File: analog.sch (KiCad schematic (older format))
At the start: 17 parts

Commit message: Erste fertige Version
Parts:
- removed D? (x2): D_Small, symbol Device:D_Small
- removed J?: Conn_02x04_Counter_Clockwise, symbol Connector_Generic:Conn_02x04_Counter_Clockwise
- added D? (x2): D_Schottky_Small, symbol Device:D_Schottky_Small
- added J?: Conn_02x05_Odd_Even, symbol Connector_Generic:Conn_02x05_Odd_Even
- added R? (x2): 10k, symbol Device:R_Small
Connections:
- net labels added: +BATT
- wire segments 43 -> 49
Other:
- moved on the sheet: R?
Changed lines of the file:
@@
 $Descr A4 11693 8268
 encoding utf-8
-Sheet 10 10
+Sheet 9 10
 Title ""
 Date ""
@@
 Wire Wire Line
 	5300 2100 3100 2100
-Wire Wire Line
-	3000 2000 5300 2000
 Connection ~ 3000 2000
-Text HLabel 6050 4750 2    50   UnSpc ~ 0
+Text HLabel 6050 4850 2    50   UnSpc ~ 0
 analog
 $Comp
@@
 	2650 4800 2650 5050
 $Comp
-L Connector_Generic:Conn_02x04_Counter_Clockwise J?
-U 1 1 5F03AAFB
-P 5150 4550
-F 0 "J?" H 5200 4867 50  0000 C CNN
-F 1 "Conn_02x04_Counter_Clockwise" H 5200 4776 50  0000 C CNN
-F 2 "" H 5150 4550 50  0001 C CNN
-F 3 "~" H 5150 4550 50  0001 C CNN
-	1    5150 4550
-	1    0    0    -1
-$EndComp
-Wire Wire Line
-	5450 4450 5450 4550
-Wire Wire Line
-	5450 4750 6050 4750
-Connection ~ 5450 4550
-Wire Wire Line
-	5450 4550 5450 4650
-Connection ~ 5450 4650
-Wire Wire Line
-	5450 4650 5450 4750
-Connection ~ 5450 4750
-$Comp
 L power:+3.3V #PWR?
 U 1 1 5F040190
-P 3550 4100
-F 0 "#PWR?" H 3550 3950 50  0001 C CNN
-F 1 "+3.3V" H 3565 4273 50  0000 C CNN
-F 2 "" H 3550 4100 50  0001 C CNN
-F 3 "" H 3550 4100 50  0001 C CNN
-	1    3550 4100
+P 3400 4100
+F 0 "#PWR?" H 3400 3950 50  0001 C CNN
+F 1 "+3.3V" H 3415 4273 50  0000 C CNN
+F 2 "" H 3400 4100 50  0001 C CNN
+F 3 "" H 3400 4100 50  0001 C CNN
+	1    3400 4100
 	1    0    0    -1
 $EndComp
@@
 L power:GND #PWR?
 U 1 1 5F04055D
-P 4000 5050
-F 0 "#PWR?" H 4000 4800 50  0001 C CNN
-F 1 "GND" H 4005 4877 50  0000 C CNN
-F 2 "" H 4000 5050 50  0001 C CNN
-F 3 "" H 4000 5050 50  0001 C CNN
-	1    4000 5050
-	1    0    0    -1
-$EndComp
-Wire Wire Line
-	4000 5050 4000 4550
-Wire Wire Line
-	4000 4550 4950 4550
+P 4450 5050
+F 0 "#PWR?" H 4450 4800 50  0001 C CNN
+F 1 "GND" H 4455 4877 50  0000 C CNN
+F 2 "" H 4450 5050 50  0001 C CNN
+F 3 "" H 4450 5050 50  0001 C CNN
+	1    4450 5050
+	1    0    0    -1
+$EndComp
+Wire Wire Line
+	4450 5050 4450 4850
 $Comp
 L Device:R_Small R?
 U 1 1 5F04265B
-P 3550 4250
-F 0 "R?" H 3609 4296 50  0000 L CNN
-F 1 "10k" H 3609 4205 50  0000 L CNN
-F 2 "" H 3550 4250 50  0001 C CNN
-F 3 "~" H 3550 4250 50  0001 C CNN
-	1    3550 4250
+P 3400 4250
+F 0 "R?" H 3459 4296 50  0000 L CNN
+F 1 "10k" H 3459 4205 50  0000 L CNN
+F 2 "" H 3400 4250 50  0001 C CNN
+F 3 "~" H 3400 4250 50  0001 C CNN
+	1    3400 4250
 	1    0    0    -1
 $EndComp
@@
 L Device:R_Small R?
 U 1 1 5F04298B
-P 3550 4800
-F 0 "R?" H 3609 4846 50  0000 L CNN
-F 1 "10k" H 3609 4755 50  0000 L CNN
-F 2 "" H 3550 4800 50  0001 C CNN
-F 3 "~" H 3550 4800 50  0001 C CNN
-	1    3550 4800
-	1    0    0    -1
-$EndComp
-Wire Wire Line
-	3550 4350 3550 4450
-Wire Wire Line
-	4950 4450 3550 4450
-Connection ~ 3550 4450
-Wire Wire Line
-	3550 4450 3550 4700
-Wire Wire Line
-	3550 4100 3550 4150
+P 3400 4800
+F 0 "R?" H 3459 4846 50  0000 L CNN
+F 1 "10k" H 3459 4755 50  0000 L CNN
+F 2 "" H 3400 4800 50  0001 C CNN
+F 3 "~" H 3400 4800 50  0001 C CNN
+	1    3400 4800
+	1    0    0    -1
+$EndComp
+Wire Wire Line
+	3400 4350 3400 4450
+Connection ~ 3400 4450
+Wire Wire Line
+	3400 4450 3400 4700
+Wire Wire Line
+	3400 4100 3400 4150
 Wire Wire Line
 	2650 4350 2650 4500
-Wire Wire Line
-	2800 4650 4950 4650
 $Comp
 L power:GND #PWR?
 U 1 1 5F051697
-P 3550 5050
-F 0 "#PWR?" H 3550 4800 50  0001 C CNN
-F 1 "GND" H 3555 4877 50  0000 C CNN
-F 2 "" H 3550 5050 50  0001 C CNN
-F 3 "" H 3550 5050 50  0001 C CNN
-	1    3550 5050
-	1    0    0    -1
-$EndComp
-Wire Wire Line
-	3550 5050 3550 4900
+P 3400 5050
+F 0 "#PWR?" H 3400 4800 50  0001 C CNN
+F 1 "GND" H 3405 4877 50  0000 C CNN
+F 2 "" H 3400 5050 50  0001 C CNN
+F 3 "" H 3400 5050 50  0001 C CNN
+	1    3400 5050
+	1    0    0    -1
+$EndComp
+Wire Wire Line
+	3400 5050 3400 4900
 $Comp
 L Device:R_Small R?
@@
 	1    0    0    -1
 $EndComp
-$Comp
-L Device:D_Small D?
-U 1 1 5F05DB9E
-P 3250 5650
-F 0 "D?" V 3204 5720 50  0000 L CNN
-F 1 "D_Small" V 3295 5720 50  0000 L CNN
-F 2 "" V 3250 5650 50  0001 C CNN
-F 3 "~" V 3250 5650 50  0001 C CNN
-	1    3250 5650
-	0    1    1    0
-$EndComp
-$Comp
-L Device:D_Small D?
-U 1 1 5F05E873
-P 3250 6050
-F 0 "D?" V 3204 6120 50  0000 L CNN
-F 1 "D_Small" V 3295 6120 50  0000 L CNN
-F 2 "" V 3250 6050 50  0001 C CNN
-F 3 "~" V 3250 6050 50  0001 C CNN
-	1    3250 6050
-	0    1    1    0
-$EndComp
 Wire Wire Line
 	3100 5850 3250 5850
@@
 $EndComp
 Wire Wire Line
-	3250 5850 4500 5850
-Wire Wire Line
-	4500 5850 4500 4750
-Wire Wire Line
-	4500 4750 4950 4750
+	3250 5850 4000 5850
+Wire Wire Line
+	4000 5850 4000 4750
 Wire Wire Line
 	2250 5850 2650 5850
@@
 	1    0    0    -1
 $EndComp
+$Comp
+L Connector_Generic:Conn_02x05_Odd_Even J?
+U 1 1 5F2EDB44
+P 5150 4650
+F 0 "J?" H 5200 5067 50  0000 C CNN
+F 1 "Conn_02x05_Odd_Even" H 5200 4976 50  0000 C CNN
+F 2 "" H 5150 4650 50  0001 C CNN
+F 3 "~" H 5150 4650 50  0001 C CNN
+	1    5150 4650
+	1    0    0    -1
+$EndComp
+Wire Wire Line
+	5450 4650 5450 4750
+Connection ~ 5450 4750
+Wire Wire Line
+	5450 4450 5450 4550
+Wire Wire Line
+	5450 4750 5450 4850
+Connection ~ 5450 4550
+Wire Wire Line
+	5450 4550 5450 4650
+Connection ~ 5450 4650
+Wire Wire Line
+	5450 4850 6050 4850
+Connection ~ 5450 4850
+$Comp
+L Device:R_Small R?
+U 1 1 5F2F92B1
+P 3000 4250
+F 0 "R?" H 3059 4296 50  0000 L CNN
+F 1 "10k" H 3059 4205 50  0000 L CNN
+F 2 "" H 3000 4250 50  0001 C CNN
+F 3 "~" H 3000 4250 50  0001 C CNN
+	1    3000 4250
+	1    0    0    -1
+$EndComp
+$Comp
+L Device:R_Small R?
+U 1 1 5F2F92B7
+P 3000 4800
+F 0 "R?" H 3059 4846 50  0000 L CNN
+F 1 "10k" H 3059 4755 50  0000 L CNN
+F 2 "" H 3000 4800 50  0001 C CNN
+F 3 "~" H 3000 4800 50  0001 C CNN
+	1    3000 4800
+	1    0    0    -1
+$EndComp
+Wire Wire Line
+	3000 4100 3000 4150
+$Comp
+L power:GND #PWR?
+U 1 1 5F2F92C3
+P 3000 5050
+F 0 "#PWR?" H 3000 4800 50  0001 C CNN
+F 1 "GND" H 3005 4877 50  0000 C CNN
+F 2 "" H 3000 5050 50  0001 C CNN
+F 3 "" H 3000 5050 50  0001 C CNN
+	1    3000 5050
+	1    0    0    -1
+$EndComp
+Wire Wire Line
+	3000 5050 3000 4900
+Wire Wire Line
+	3000 4350 3000 4550
+Wire Wire Line
+	4450 4850 4950 4850
+Wire Wire Line
+	4000 4750 4950 4750
+Wire Wire Line
+	3400 4450 4950 4450
+Wire Wire Line
+	4950 4550 3000 4550
+Connection ~ 3000 4550
+Wire Wire Line
+	3000 4550 3000 4700
+$Comp
+L power:+BATT #PWR?
+U 1 1 5F30C3D0
+P 3000 4100
+F 0 "#PWR?" H 3000 3950 50  0001 C CNN
+F 1 "+BATT" H 3015 4273 50  0000 C CNN
+F 2 "" H 3000 4100 50  0001 C CNN
+F 3 "" H 3000 4100 50  0001 C CNN
+	1    3000 4100
+	1    0    0    -1
+$EndComp
+$Comp
+L Device:D_Schottky_Small D?
+U 1 1 5F30DD96
+P 3250 6050
+F 0 "D?" V 3250 6120 50  0000 L CNN
+F 1 "D_Schottky_Small" V 3295 6120 50  0001 L CNN
+F 2 "" V 3250 6050 50  0001 C CNN
+F 3 "~" V 3250 6050 50  0001 C CNN
+	1    3250 6050
+	0    1    1    0
+$EndComp
+$Comp
+L Device:D_Schottky_Small D?
+U 1 1 5F30E51F
+P 3250 5650
+F 0 "D?" V 3250 5720 50  0000 L CNN
+F 1 "D_Schottky_Small" V 3295 5720 50  0001 L CNN
+F 2 "" V 3250 5650 50  0001 C CNN
+F 3 "~" V 3250 5650 50  0001 C CNN
+	1    3250 5650
+	0    1    1    0
+$EndComp
+Wire Wire Line
+	2800 4650 4950 4650
+Wire Wire Line
+	3000 2000 5300 2000
 $EndSCHEMATC

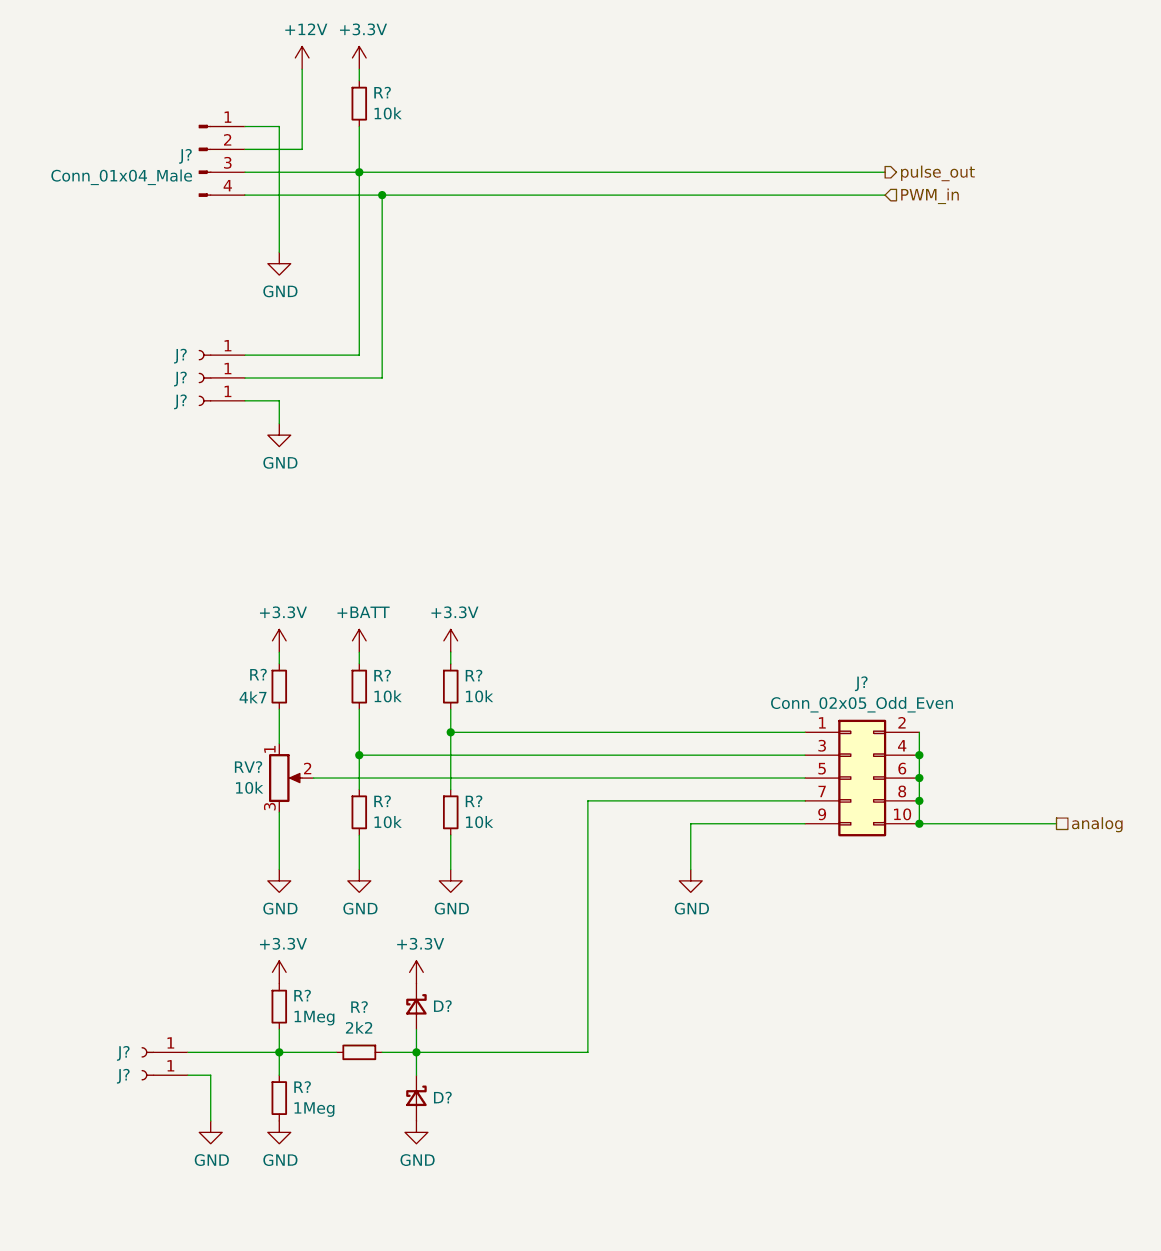
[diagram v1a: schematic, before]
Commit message: Bauteile grob platziert
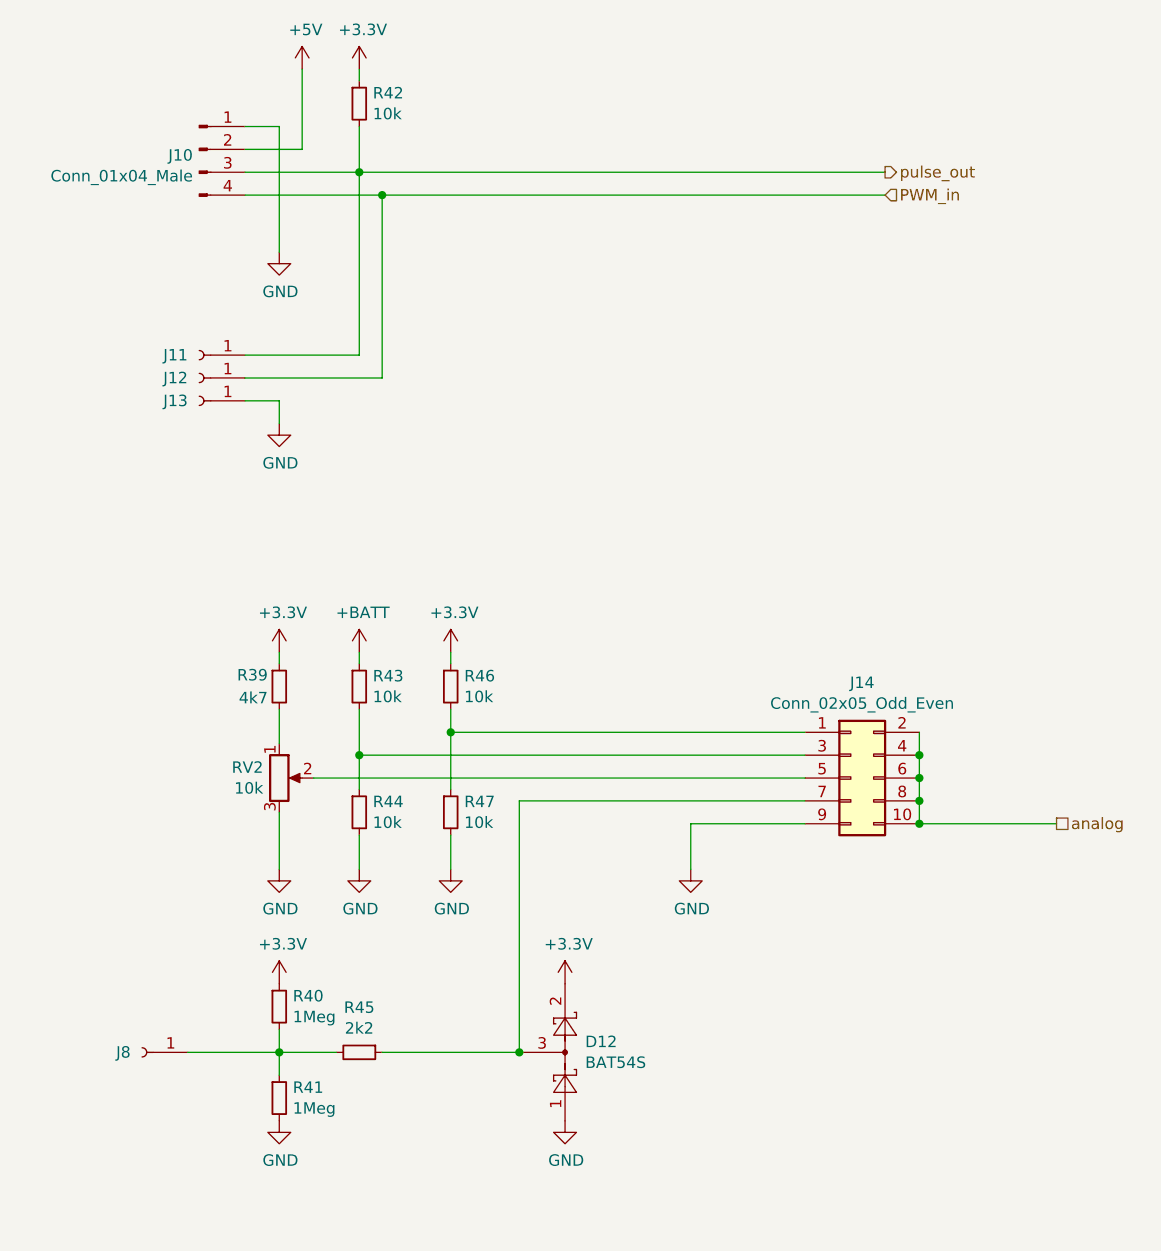
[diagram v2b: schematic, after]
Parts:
- removed D? (x2): D_Schottky_Small, symbol Device:D_Schottky_Small
- removed J?: Conn_01x01_Female, symbol Connector:Conn_01x01_Female
- added D12: BAT54S, Package_TO_SOT_SMD:SOT-23, symbol Diode:BAT54S
- J10: renamed from J?; footprint (none) -> Connector_Molex:Molex_KK-254_AE-6410-04A_1x04_P2.54mm_Vertical
- J11, J12, J13, J8: renamed from J?; footprint (none) -> HS-Wismar:2mm_Socket
- J14: renamed from J?; footprint (none) -> Connector_PinHeader_2.54mm:PinHeader_2x05_P2.54mm_Vertical
- R39, R40, R41, R42, R43, R44, R45, R46, R47: renamed from R?; footprint (none) -> Resistor_SMD:R_0603_1608Metric_Pad1.05x0.95mm_HandSolder
- RV2: renamed from RV?; footprint (none) -> Potentiometer_THT:Potentiometer_Alps_RK09K_Single_Vertical
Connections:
- net +3V3: now also D12.2
- net GND: now also D12.1
- net at J14.7 (Pin_7), R45.1: now also D12.3
- net +12V renamed +5V

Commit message: Alle Bauteile platziert
Alle Bauteile sind grob plaziert.
Einige Bauteile sollten noch umplaziert werden (u. a. die Jumper links neben Groov-Con, RGB-LED,).
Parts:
- D12: symbol Diode:BAT54S -> MCT_Labor_5529-rescue:BAT54S-Diode
- J10: symbol Connector:Conn_01x04_Male -> MCT_Labor_5529-rescue:Conn_01x04_Male-Connector
- J11, J12, J13, J8: symbol Connector:Conn_01x01_Female -> MCT_Labor_5529-rescue:Conn_01x01_Female-Connector
- J14: symbol Connector_Generic:Conn_02x05_Odd_Even -> MCT_Labor_5529-rescue:Conn_02x05_Odd_Even-Connector_Generic
- R39, R40, R41, R42, R43, R44, R45, R46, R47: symbol Device:R_Small -> MCT_Labor_5529-rescue:R_Small-Device
- RV2: symbol Device:R_POT -> MCT_Labor_5529-rescue:R_POT-Device
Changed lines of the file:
@@
 $EndDescr
 $Comp
-L Connector:Conn_01x04_Male J10
+L MCT_Labor_5529-rescue:Conn_01x04_Male-Connector J10
 U 1 1 5F032368
 P 2300 1900
@@
 $EndComp
 $Comp
-L power:GND #PWR0192
+L MCT_Labor_5529-rescue:GND-power #PWR0192
 U 1 1 5F03480E
 P 2650 2350
@@
 	2650 1800 2650 2350
 $Comp
-L Device:R_Small R42
+L MCT_Labor_5529-rescue:R_Small-Device R42
 U 1 1 5F035967
 P 3000 1700
@@
 $EndComp
 $Comp
-L power:+3.3V #PWR0193
+L MCT_Labor_5529-rescue:+3.3V-power #PWR0193
 U 1 1 5F035D2B
 P 3000 1550
@@
 analog
 $Comp
-L Device:R_POT RV2
+L MCT_Labor_5529-rescue:R_POT-Device RV2
 U 1 1 5F0370CA
 P 2650 4650
@@
 $EndComp
 $Comp
-L power:+3.3V #PWR0194
+L MCT_Labor_5529-rescue:+3.3V-power #PWR0194
 U 1 1 5F038833
 P 2650 4100
@@
 $EndComp
 $Comp
-L power:GND #PWR0195
+L MCT_Labor_5529-rescue:GND-power #PWR0195
 U 1 1 5F038AC9
 P 2650 5050
@@
 $EndComp
 $Comp
-L Device:R_Small R39
+L MCT_Labor_5529-rescue:R_Small-Device R39
 U 1 1 5F0393AE
 P 2650 4250
@@
 	2650 4800 2650 5050
 $Comp
-L power:+3.3V #PWR0196
+L MCT_Labor_5529-rescue:+3.3V-power #PWR0196
 U 1 1 5F040190
 P 3400 4100
@@
 $EndComp
 $Comp
-L power:GND #PWR0197
+L MCT_Labor_5529-rescue:GND-power #PWR0197
 U 1 1 5F04055D
 P 4450 5050
@@
 	4450 5050 4450 4850
 $Comp
-L Device:R_Small R46
+L MCT_Labor_5529-rescue:R_Small-Device R46
 U 1 1 5F04265B
 P 3400 4250
@@
 $EndComp
 $Comp
-L Device:R_Small R47
+L MCT_Labor_5529-rescue:R_Small-Device R47
 U 1 1 5F04298B
 P 3400 4800
@@
 	2650 4350 2650 4500
 $Comp
-L power:GND #PWR0198
+L MCT_Labor_5529-rescue:GND-power #PWR0198
 U 1 1 5F051697
 P 3400 5050
@@
 	3400 5050 3400 4900
 $Comp
-L Device:R_Small R45
+L MCT_Labor_5529-rescue:R_Small-Device R45
 U 1 1 5F058350
 P 3000 5850
@@
 	2650 5850 2650 5950
 $Comp
-L power:+3.3V #PWR0199
+L MCT_Labor_5529-rescue:+3.3V-power #PWR0199
 U 1 1 5F05B56F
 P 2650 5550
@@
 $EndComp
 $Comp
-L power:GND #PWR0200
+L MCT_Labor_5529-rescue:GND-power #PWR0200
 U 1 1 5F05C651
 P 2650 6150
@@
 $EndComp
 $Comp
-L power:+3.3V #PWR0201
+L MCT_Labor_5529-rescue:+3.3V-power #PWR0201
 U 1 1 5F05F76F
 P 3900 5550
@@
 $EndComp
 $Comp
-L power:GND #PWR0202
+L MCT_Labor_5529-rescue:GND-power #PWR0202
 U 1 1 5F05FB53
 P 3900 6150
@@
 	2250 5850 2650 5850
 $Comp
-L Device:R_Small R41
+L MCT_Labor_5529-rescue:R_Small-Device R41
 U 1 1 5F058029
 P 2650 6050
@@
 $EndComp
 $Comp
-L Device:R_Small R40
+L MCT_Labor_5529-rescue:R_Small-Device R40
 U 1 1 5F057D1E
 P 2650 5650
@@
 $EndComp
 $Comp
-L Connector:Conn_01x01_Female J8
+L MCT_Labor_5529-rescue:Conn_01x01_Female-Connector J8
 U 1 1 5F0751E3
 P 2050 5850
@@
 $EndComp
 $Comp
-L Connector:Conn_01x01_Female J11
+L MCT_Labor_5529-rescue:Conn_01x01_Female-Connector J11
 U 1 1 5F076A07
 P 2300 2800
@@
 $EndComp
 $Comp
-L Connector:Conn_01x01_Female J12
+L MCT_Labor_5529-rescue:Conn_01x01_Female-Connector J12
 U 1 1 5F077288
 P 2300 2900
@@
 $EndComp
 $Comp
-L Connector:Conn_01x01_Female J13
+L MCT_Labor_5529-rescue:Conn_01x01_Female-Connector J13
 U 1 1 5F077A2E
 P 2300 3000
@@
 	2650 3000 2650 3100
 $Comp
-L power:GND #PWR0204
+L MCT_Labor_5529-rescue:GND-power #PWR0204
 U 1 1 5F07A1D6
 P 2650 3100
@@
 $EndComp
 $Comp
-L Connector_Generic:Conn_02x05_Odd_Even J14
+L MCT_Labor_5529-rescue:Conn_02x05_Odd_Even-Connector_Generic J14
 U 1 1 5F2EDB44
 P 5150 4650
@@
 Connection ~ 5450 4850
 $Comp
-L Device:R_Small R43
+L MCT_Labor_5529-rescue:R_Small-Device R43
 U 1 1 5F2F92B1
 P 3000 4250
@@
 $EndComp
 $Comp
-L Device:R_Small R44
+L MCT_Labor_5529-rescue:R_Small-Device R44
 U 1 1 5F2F92B7
 P 3000 4800
@@
 	3000 4100 3000 4150
 $Comp
-L power:GND #PWR0205
+L MCT_Labor_5529-rescue:GND-power #PWR0205
 U 1 1 5F2F92C3
 P 3000 5050
@@
 	3000 4550 3000 4700
 $Comp
-L power:+BATT #PWR0206
+L MCT_Labor_5529-rescue:+BATT-power #PWR0206
 U 1 1 5F30C3D0
 P 3000 4100
@@
 	3000 2000 5300 2000
 $Comp
-L Diode:BAT54S D12
+L MCT_Labor_5529-rescue:BAT54S-Diode D12
 U 1 1 5F0A013B
 P 3900 5850
@@
 	3100 5850 3700 5850
 $Comp
-L power:+5V #PWR0191
+L MCT_Labor_5529-rescue:+5V-power #PWR0191
 U 1 1 5F2DF455
 P 2750 1550

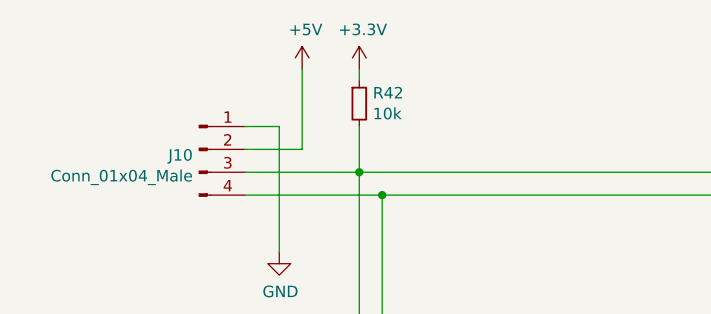
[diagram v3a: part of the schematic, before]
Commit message: Anpassungen am Lüfteranschluss und den LEDs
-Lüfteranschluss verändert
 -> 12V-Versorgung eingefügt
-LED & LCD auf 3,3V umgestellt
 -> Ladungspunpe für neg. Kontrastspannung
-keine 5V Versorgung mehr
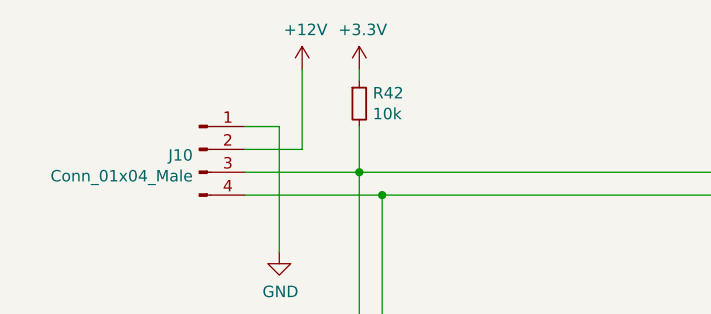
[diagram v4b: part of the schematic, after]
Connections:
- net +5V renamed +12V
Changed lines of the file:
@@
 	3100 5850 3700 5850
 $Comp
-L MCT_Labor_5529-rescue:+5V-power #PWR0191
-U 1 1 5F2DF455
+L power:+12V #PWR01
+U 1 1 5F28DEAC
 P 2750 1550
-F 0 "#PWR0191" H 2750 1400 50  0001 C CNN
-F 1 "+5V" H 2765 1723 50  0000 C CNN
+F 0 "#PWR01" H 2750 1400 50  0001 C CNN
+F 1 "+12V" H 2765 1723 50  0000 C CNN
 F 2 "" H 2750 1550 50  0001 C CNN
 F 3 "" H 2750 1550 50  0001 C CNN
